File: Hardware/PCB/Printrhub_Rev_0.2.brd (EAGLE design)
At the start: 75 x 60.5 mm, 67 parts, among them J1 DM3D-SF, SW1 SPST_TACT-KMR2, SW2 SPST_TACT-KMR2, U1 MK20DX256VLH7, U2 AP1117E, U3 MAX308-SOT23, Y2 16Mhz/8pF

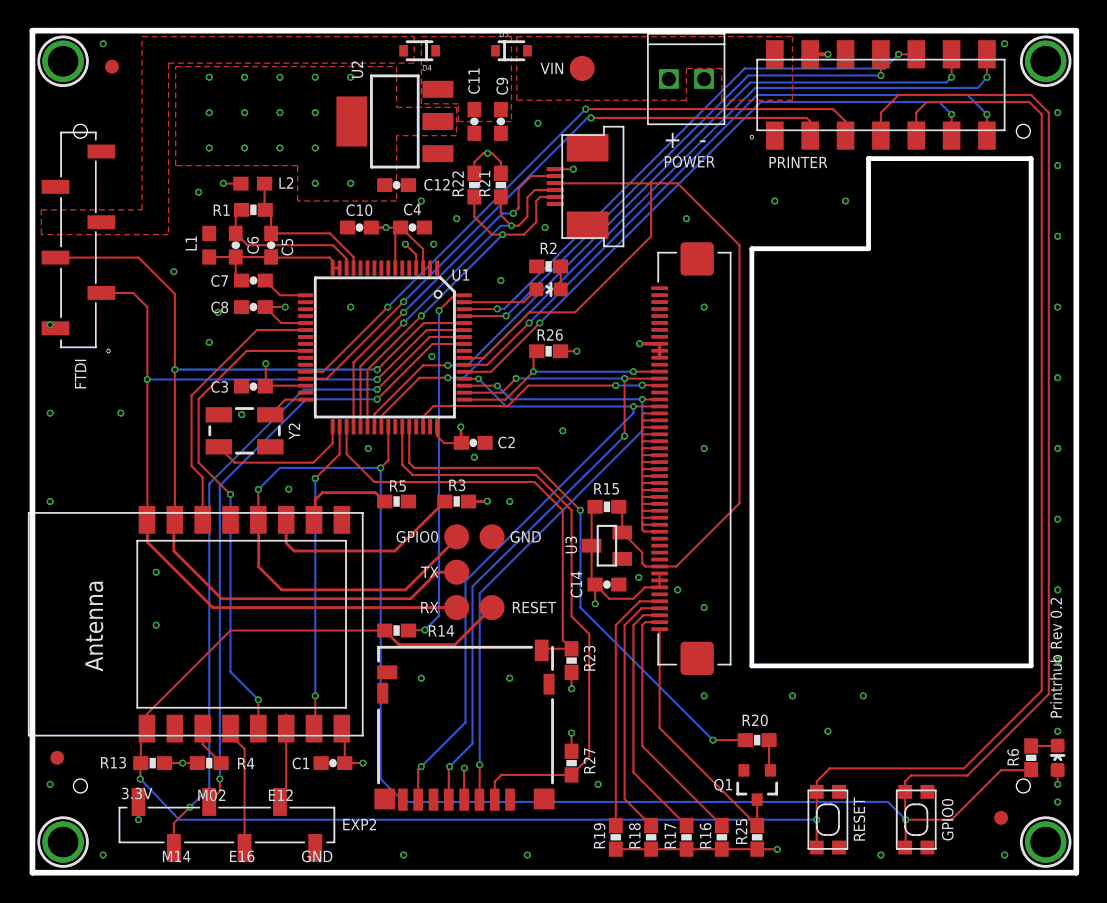
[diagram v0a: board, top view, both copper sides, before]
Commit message: Fixed a small bug in Rev 0.2 of the Printrhub PCB
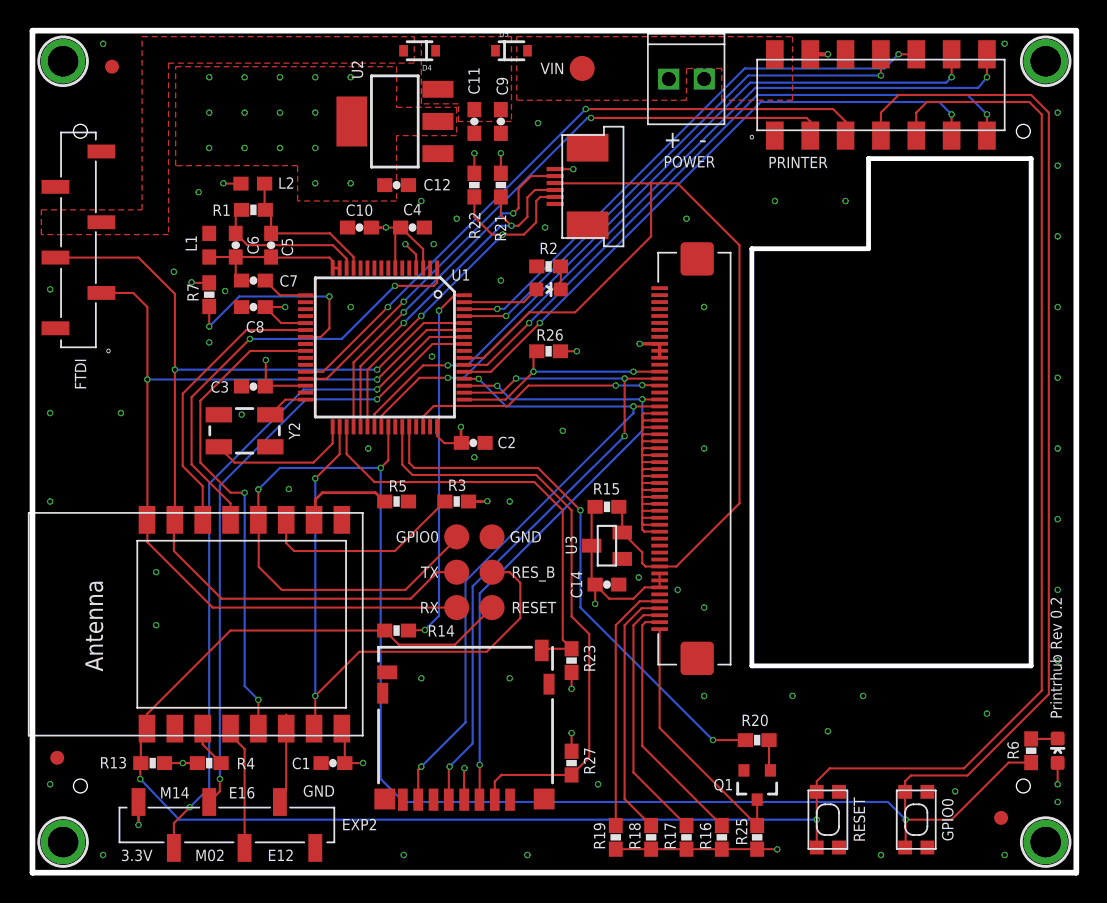
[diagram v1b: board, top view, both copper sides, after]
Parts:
- added R7: 0, appfruits:0603-RES
- added RES_B: TPV-SMD-18RN, appfruits:SMD-18RN
- moved LED1 0.51 mm to (73.7, 8.76)
- moved R6 0.51 mm to (71.8, 8.76)
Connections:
- new net N$3: R7.1, U1.23
- net 3.3V: now also R7.2
- net ESP_GPIO5: now also U1.1
- net RESET_B: now also RES_B.TP
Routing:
- net ESP_GPIO5: track 0.00 -> 32.1 mm, vias 0 -> 2
- net RESET_B: track 22.5 -> 44.4 mm
- net N$3: track 0.00 -> 15.2 mm, vias 0 -> 2
- net 3.3V: track 74.1 -> 75.4 mm, vias 35 -> 37
- net SWD_CLK: track 19.4 -> 20.4 mm
- net GND: vias 59 -> 60
